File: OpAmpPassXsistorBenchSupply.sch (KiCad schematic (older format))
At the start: 55 parts

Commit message: breaking vcc out into sub sheets
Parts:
- removed C? (x3): 0.1uF, ~, symbol C_CER
- removed C? (x2): 10uF, ~, symbol C_EL
- removed C? (x2): 1000uF, ~, symbol C_EL
- removed C? (x2): 4.7uF, ~, symbol C_MKS2
- removed CON?: 2.5x5.5mm, ~, symbol BARREL_JACK
- removed CON?: 2.1x5.5mm, ~, symbol BARREL_JACK
- removed D? (x2): 1N4148, ~, symbol DIODE
- removed L?: 100uH, ~, symbol INDUCTOR
- removed R? (x2): R_0W25_1PCT, ~, symbol R_0W25_1PCT
- removed R? (x8): 1, ~, symbol R_0W5
- removed U?: LM317, ~, symbol LM317
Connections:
- net labels removed: Vcc_filt, Vcc_raw
- wire segments 158 -> 103
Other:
- note removed: "0.5 Ohm, 4 Watt\n(8 Amp limit)"
- note removed: "positive supply"

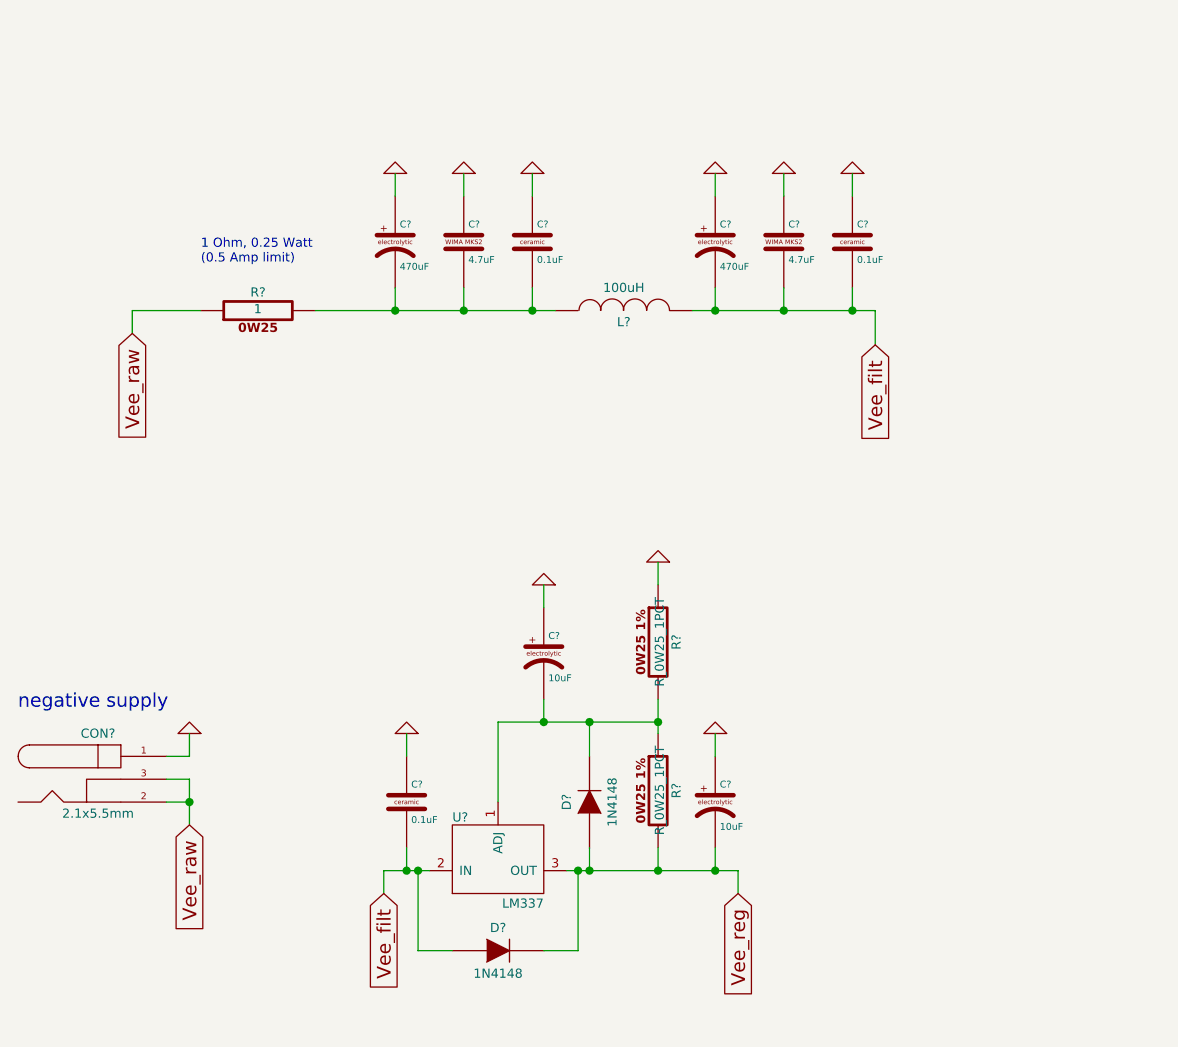
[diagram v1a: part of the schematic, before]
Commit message: breaking Vee out into sub sheets
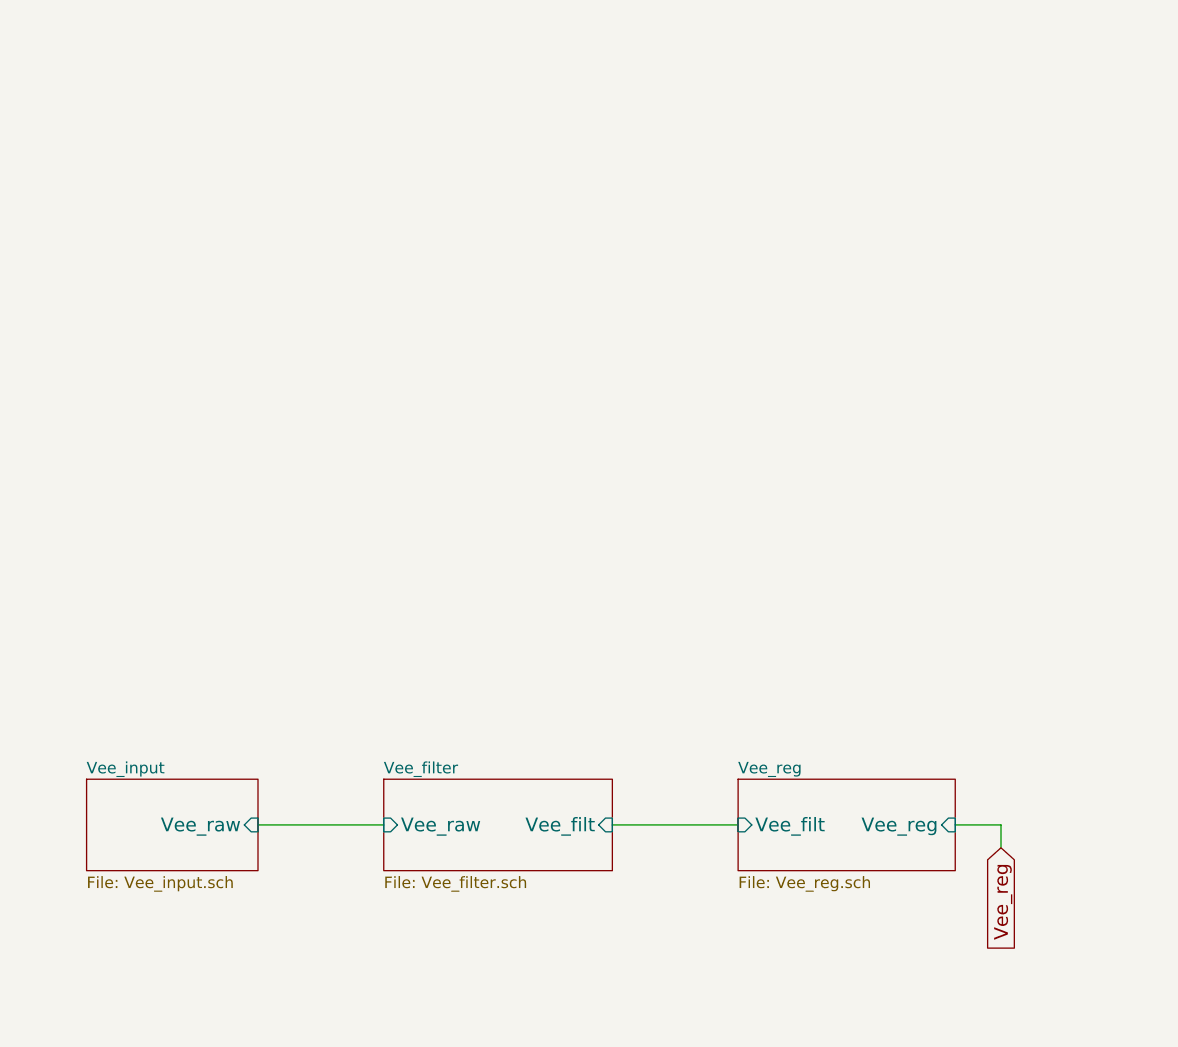
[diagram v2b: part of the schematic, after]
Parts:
- removed C? (x3): 0.1uF, ~, symbol C_CER
- removed C? (x2): 10uF, ~, symbol C_EL
- removed C? (x2): 470uF, ~, symbol C_EL
- removed C? (x2): 4.7uF, ~, symbol C_MKS2
- removed CON?: 2.1x5.5mm, ~, symbol BARREL_JACK
- removed D? (x2): 1N4148, ~, symbol DIODE
- removed L?: 100uH, ~, symbol INDUCTOR
- removed R? (x2): R_0W25_1PCT, ~, symbol R_0W25_1PCT
- removed R?: 1, ~, symbol R_0W25
- removed U?: LM337, ~, symbol LM337
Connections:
- net labels removed: Vee_filt, Vee_raw
- wire segments 103 -> 64
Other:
- note removed: "1 Ohm, 0.25 Watt\n(0.5 Amp limit)"
- note removed: "negative supply"

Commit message: breaking out additional subsheets.  specifying transistor values.
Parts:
- removed Q? (x4): NPN_EBC, ~, symbol NPN_EBC
- removed Q?: PNP_EBC, ~, symbol PNP_EBC
- removed R?: R_0W25, ~, symbol R_0W25
- removed R?: R_0W5_1PCT, ~, symbol R_0W5_1PCT
- added Q? (x4): 2N3904, ~, symbol 2N3904
- added R? (x4): 1k, ~, symbol R_0W25
- added U?: LM324N, symbol LM324N
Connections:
- net labels added: Tcontrol, temperature sensor
- wire segments 64 -> 67
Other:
- moved on the sheet: R?, U?, U?A

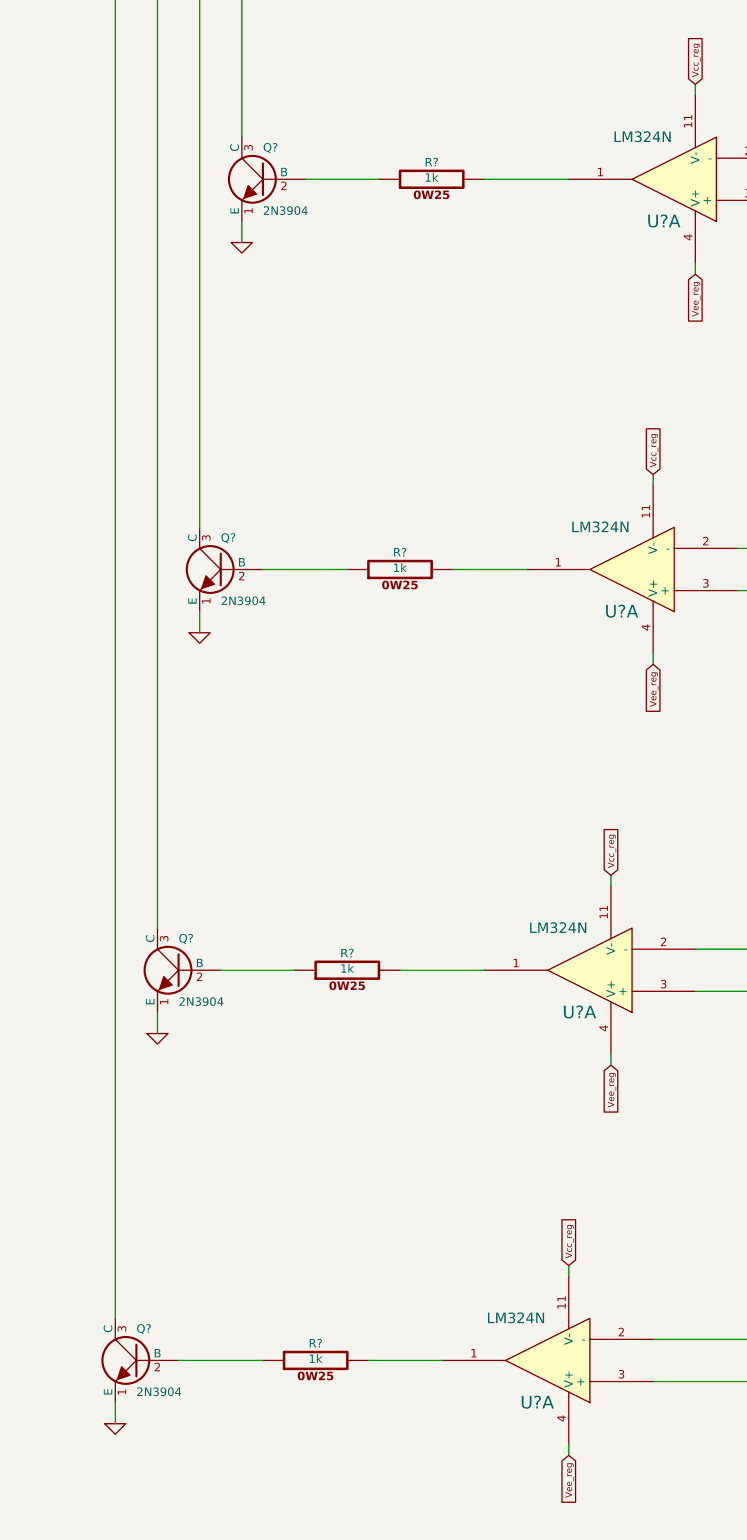
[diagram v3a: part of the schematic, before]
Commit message: adding base resistor to pnp.
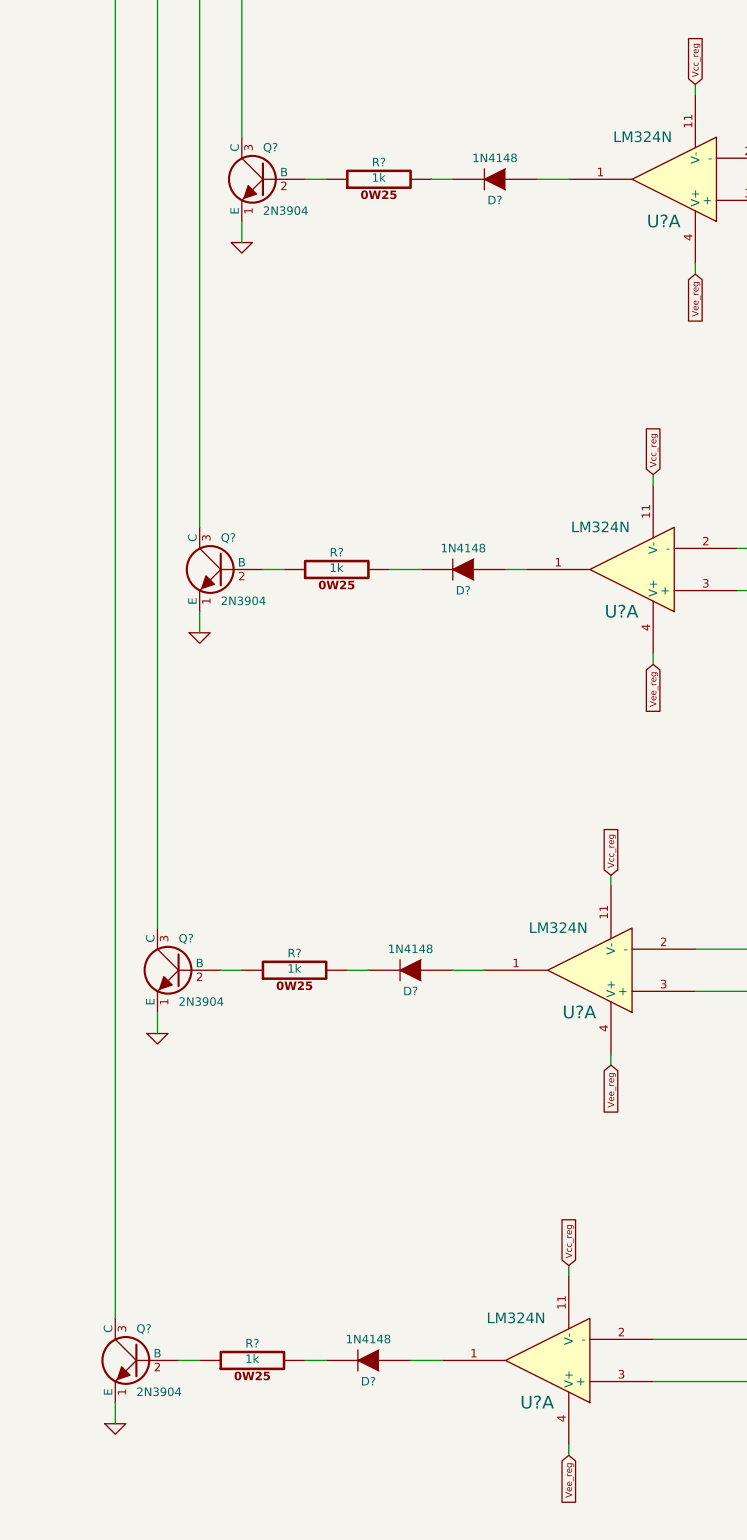
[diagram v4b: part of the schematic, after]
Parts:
- added D? (x4): 1N4148, ~, symbol DIODE
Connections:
- net at U?.1: now also D?.1 (A); no longer R?.2 (x4)
- new net: D?.2 (K), R?.2 (x4)
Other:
- moved on the sheet: R?
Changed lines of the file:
@@
 L R_0W25 R?
 U 1 1 5339674C
-P 7600 2700
-F 0 "R?" V 7680 2700 40  0000 C CNN
-F 1 "1k" V 7607 2701 40  0000 C CNN
-F 2 "~" V 7530 2700 30  0000 C CNN
-F 3 "~" H 7600 2700 30  0000 C CNN
-	1    7600 2700
+P 7350 2700
+F 0 "R?" V 7430 2700 40  0000 C CNN
+F 1 "1k" V 7357 2701 40  0000 C CNN
+F 2 "~" V 7280 2700 30  0000 C CNN
+F 3 "~" H 7350 2700 30  0000 C CNN
+	1    7350 2700
 	0    -1   -1   0
 $EndComp
@@
 L R_0W25 R?
 U 1 1 53397C58
-P 7450 4550
-F 0 "R?" V 7530 4550 40  0000 C CNN
-F 1 "1k" V 7457 4551 40  0000 C CNN
-F 2 "~" V 7380 4550 30  0000 C CNN
-F 3 "~" H 7450 4550 30  0000 C CNN
-	1    7450 4550
+P 7150 4550
+F 0 "R?" V 7230 4550 40  0000 C CNN
+F 1 "1k" V 7157 4551 40  0000 C CNN
+F 2 "~" V 7080 4550 30  0000 C CNN
+F 3 "~" H 7150 4550 30  0000 C CNN
+	1    7150 4550
 	0    -1   -1   0
 $EndComp
@@
 L R_0W25 R?
 U 1 1 53398285
-P 7200 6450
-F 0 "R?" V 7280 6450 40  0000 C CNN
-F 1 "1k" V 7207 6451 40  0000 C CNN
-F 2 "~" V 7130 6450 30  0000 C CNN
-F 3 "~" H 7200 6450 30  0000 C CNN
-	1    7200 6450
+P 6950 6450
+F 0 "R?" V 7030 6450 40  0000 C CNN
+F 1 "1k" V 6957 6451 40  0000 C CNN
+F 2 "~" V 6880 6450 30  0000 C CNN
+F 3 "~" H 6950 6450 30  0000 C CNN
+	1    6950 6450
 	0    -1   -1   0
 $EndComp
@@
 L R_0W25 R?
 U 1 1 53398885
-P 7050 8300
-F 0 "R?" V 7130 8300 40  0000 C CNN
-F 1 "1k" V 7057 8301 40  0000 C CNN
-F 2 "~" V 6980 8300 30  0000 C CNN
-F 3 "~" H 7050 8300 30  0000 C CNN
-	1    7050 8300
+P 6750 8300
+F 0 "R?" V 6830 8300 40  0000 C CNN
+F 1 "1k" V 6757 8301 40  0000 C CNN
+F 2 "~" V 6680 8300 30  0000 C CNN
+F 3 "~" H 6750 8300 30  0000 C CNN
+	1    6750 8300
 	0    -1   -1   0
 $EndComp
-Wire Wire Line
-	7000 2700 7350 2700
-Wire Wire Line
-	7850 2700 8250 2700
-Wire Wire Line
-	6800 4550 7200 4550
-Wire Wire Line
-	7700 4550 8050 4550
-Wire Wire Line
-	6600 6450 6950 6450
-Wire Wire Line
-	7450 6450 7850 6450
-Wire Wire Line
-	6400 8300 6800 8300
-Wire Wire Line
-	7300 8300 7650 8300
 Wire Wire Line
 	4750 2400 4950 2400
@@
 Text GLabel 9750 4200 1    30   Input ~ 0
 Vcc_reg
+$Comp
+L DIODE D?
+U 1 1 533AC637
+P 7900 2700
+F 0 "D?" H 7900 2800 40  0000 C CNN
+F 1 "1N4148" H 7900 2600 40  0000 C CNN
+F 2 "~" H 7900 2700 60  0000 C CNN
+F 3 "~" H 7900 2700 60  0000 C CNN
+	1    7900 2700
+	-1   0    0    1
+$EndComp
+Wire Wire Line
+	7000 2700 7100 2700
+Wire Wire Line
+	7600 2700 7700 2700
+Wire Wire Line
+	8100 2700 8250 2700
+$Comp
+L DIODE D?
+U 1 1 533AE5CA
+P 7750 4550
+F 0 "D?" H 7750 4650 40  0000 C CNN
+F 1 "1N4148" H 7750 4450 40  0000 C CNN
+F 2 "~" H 7750 4550 60  0000 C CNN
+F 3 "~" H 7750 4550 60  0000 C CNN
+	1    7750 4550
+	-1   0    0    1
+$EndComp
+$Comp
+L DIODE D?
+U 1 1 533AE5D0
+P 7500 6450
+F 0 "D?" H 7500 6550 40  0000 C CNN
+F 1 "1N4148" H 7500 6350 40  0000 C CNN
+F 2 "~" H 7500 6450 60  0000 C CNN
+F 3 "~" H 7500 6450 60  0000 C CNN
+	1    7500 6450
+	-1   0    0    1
+$EndComp
+$Comp
+L DIODE D?
+U 1 1 533AE8A6
+P 7300 8300
+F 0 "D?" H 7300 8400 40  0000 C CNN
+F 1 "1N4148" H 7300 8200 40  0000 C CNN
+F 2 "~" H 7300 8300 60  0000 C CNN
+F 3 "~" H 7300 8300 60  0000 C CNN
+	1    7300 8300
+	-1   0    0    1
+$EndComp
+Wire Wire Line
+	6800 4550 6900 4550
+Wire Wire Line
+	7400 4550 7550 4550
+Wire Wire Line
+	7950 4550 8050 4550
+Wire Wire Line
+	6600 6450 6700 6450
+Wire Wire Line
+	7200 6450 7300 6450
+Wire Wire Line
+	7700 6450 7850 6450
+Wire Wire Line
+	6400 8300 6500 8300
+Wire Wire Line
+	7000 8300 7100 8300
+Wire Wire Line
+	7500 8300 7650 8300
 $EndSCHEMATC

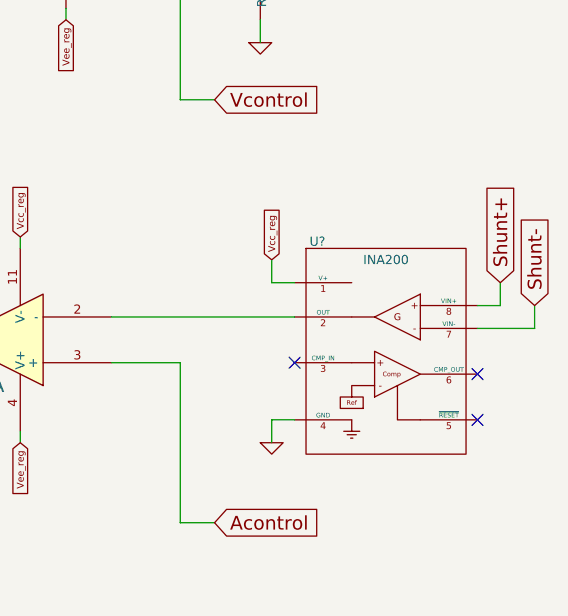
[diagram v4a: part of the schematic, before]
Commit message: WIP.  switching to INA193.  revisiting input filter.
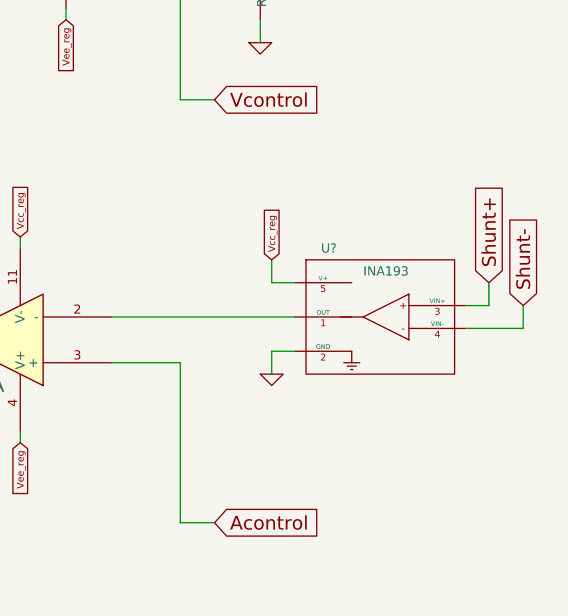
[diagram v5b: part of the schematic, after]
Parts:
- removed U?: INA200, ~, symbol INA200
- added U?: INA193, ~, symbol INA193
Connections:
- net GND: now also U?.2 (GND)
- net Shunt+: now also U?.3 (VIN+)
- net Shunt-: now also U?.4 (VIN-)
- net Vcc_reg: now also U?.5 (V+)
- net at U?.2 (-): now also U?.1 (OUT)
- no-connect marks 3 -> 0
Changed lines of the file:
@@
 Sheet 1 9
 Title ""
-Date "29 mar 2014"
+Date "4 jul 2014"
 Rev ""
 Comp ""
@@
 Wire Wire Line
 	9350 3500 9500 3500
-$Comp
-L INA200 U?
-U 1 1 53367624
-P 10250 4700
-F 0 "U?" H 9950 5280 40  0000 C CNN
-F 1 "INA200" H 10250 5200 40  0000 C CNN
-F 2 "~" H 10125 4650 60  0000 C CNN
-F 3 "~" H 10125 4650 60  0000 C CNN
-	1    10250 4700
-	1    0    0    -1
-$EndComp
 Wire Wire Line
 	9750 4200 9750 4300
@@
 L GND #PWR?
 U 1 1 533676A0
-P 9750 5000
-F 0 "#PWR?" H 9750 5000 30  0001 C CNN
-F 1 "GND" H 9750 4930 30  0001 C CNN
-F 2 "" H 9750 5000 60  0000 C CNN
-F 3 "" H 9750 5000 60  0000 C CNN
-	1    9750 5000
-	1    0    0    -1
-$EndComp
-Wire Wire Line
-	9750 5000 9750 4900
-Wire Wire Line
-	9750 4900 9850 4900
-NoConn ~ 9850 4650
-NoConn ~ 10650 4700
-NoConn ~ 10650 4900
+P 9750 4700
+F 0 "#PWR?" H 9750 4700 30  0001 C CNN
+F 1 "GND" H 9750 4630 30  0001 C CNN
+F 2 "" H 9750 4700 60  0000 C CNN
+F 3 "" H 9750 4700 60  0000 C CNN
+	1    9750 4700
+	1    0    0    -1
+$EndComp
+Wire Wire Line
+	9750 4700 9750 4600
+Wire Wire Line
+	9750 4600 9850 4600
 Text GLabel 9900 1350 1    60   Input ~ 0
 Vout
-Text GLabel 10750 4300 1    60   Input ~ 0
+Text GLabel 10700 4300 1    60   Input ~ 0
 Shunt+
-Text GLabel 10900 4400 1    60   Input ~ 0
+Text GLabel 10850 4400 1    60   Input ~ 0
 Shunt-
 Wire Wire Line
-	10650 4400 10750 4400
-Wire Wire Line
-	10750 4400 10750 4300
-Wire Wire Line
-	10650 4500 10900 4500
-Wire Wire Line
-	10900 4500 10900 4400
+	10600 4400 10700 4400
+Wire Wire Line
+	10700 4400 10700 4300
+Wire Wire Line
+	10600 4500 10850 4500
+Wire Wire Line
+	10850 4500 10850 4400
 $Comp
 L LM324N U?
@@
 Wire Wire Line
 	7500 8300 7650 8300
+$Comp
+L INA193 U?
+U 1 1 53B62EA4
+P 10250 4450
+F 0 "U?" H 10000 4750 40  0000 C CNN
+F 1 "INA193" H 10250 4650 40  0000 C CNN
+F 2 "~" H 10075 4150 60  0000 C CNN
+F 3 "~" H 10075 4150 60  0000 C CNN
+	1    10250 4450
+	1    0    0    -1
+$EndComp
 $EndSCHEMATC

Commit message: working on revamp of power supply.
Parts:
- removed D? (x4): 1N4148, ~, symbol DIODE
- removed Q? (x2): 2N3904, ~, symbol 2N3904
- removed R? (x2): 1k, ~, symbol R_0W25
- removed U? (x4): LM324N, symbol LM324N
- added C1, C3: 100uF, ~, symbol C_EL
- added C10, C11, C12, C13: 0.1uF, ~, symbol C_CER
- added C2, C4, C7, C9: 1uF, ~, symbol C_FILM
- added C5: 10uF, ~, symbol C_EL
- added C6, C8: 1000uF, ~, symbol C_EL
- added CON1: 2.5x5.5mm, ~, symbol BARREL_JACK
- added CON2: 2.1x5.5mm, ~, symbol BARREL_JACK
- added DS1: AMMETER_V, ~, symbol AMMETER_V
- added DS2: VOLTMETER, ~, symbol VOLTMETER
- added H1, H2, H3, H4: HOLE, ~, symbol HOLE
- added L1: 10uH, ~, symbol INDUCTOR
- added L2: 100uH, ~, symbol INDUCTOR
- added P1, P2: CONN_1, symbol CONN_1
- added Q3: TIP120, TO220, symbol TIP120
- added R1, R10, R11, R12, R19, R20, R21, R22, R23, R24, R25, R26, R27, R28, R5, R6, R7, R8, R9: 1, ~, symbol R_0W25_1PCT
- added R13, R14, R15, R16: 1k, ~, symbol R_0W25
- added R2: 4.7k, ~, symbol R_0W25_1PCT
- added R3, R31, R32: 47k, ~, symbol R_0W25_1PCT
- added R4: 10k, ~, symbol R_0W25_1PCT
- added RV1, RV4: 1k, ~, symbol POT_10T
- added RV2, RV3: 47k, ~, symbol POT_10T
- added SW1, SW2: SPDT, ~, symbol SPDT
- added U1: TL431, ~, symbol TL431
- added U2: 7805, ~, symbol 7805
- added U3: LM358, ~, symbol LM358
- R29: renamed from R?; value R_0W25_1PCT -> 68k
- R30: renamed from R?; value R_0W25_1PCT -> 10k
- gave numbers to parts that had none: 5
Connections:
- net labels added: Icontrol, Isense, VREF, Vcc_filt, Vsense
- net labels removed: Acontrol, Pcontrol, Tcontrol, Vee_reg, analog multiplier, temperature sensor
- wire segments 71 -> 146
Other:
- note added: "0.1 Ohm, 2.5 Watt shunt\n(5A max)"
- note added: "0.5 Ohm, 2 Watt\n(2 Amp limit)"
- note added: "1.5A = 3.0V"
- note added: "24Vout = 3.08V"
- note added: "Adjust for 3V"
- note added: "Design target: 0-24V, 0-1.5A supply"
- note added: "Output Enable"
- note added: "Power"
- note added: "Remove 50 mOhm shunt"
- note added: "target an input range of 0V - 3V"
- moved on the sheet: Q1, Q2, R17, R18, R29, R30, U4

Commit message: revision 1 being sent off to PCB house.
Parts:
- removed R1, R10, R11, R12, R7, R8, R9: 1, ~, symbol R_0W25_1PCT
- added C14, C15, C16: 0.1uF, ~, symbol C_CER
- added D1, D2: LED, ~, symbol LED
- added FB1, FB2, FB3, FB4: FERRITE_BEAD, ~, symbol FERRITE_BEAD
- added Q4, Q5: 2N3904, ~, symbol 2N3904
- added R1, R10, R11, R12, R33, R34, R7, R8, R9: 1, ~, symbol R_0W25
- added R35, R36: 220, ~, symbol R_0W25
- added R37, R38: 1k, ~, symbol R_0W25_1PCT
- L1: value 10uH -> 100uH, 100mA
- L2: value 100uH -> 100uH, 2A
- R5, R6: value 1 -> 0
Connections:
- net labels added: Base
- wire segments 146 -> 172
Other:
- note added: "All input caps 35V"
- moved on the sheet: C1, C2, C3, C4, C5, CON1, CON2, L1, R17, R18, R2, R3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
